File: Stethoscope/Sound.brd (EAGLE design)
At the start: 70 x 70 mm, 24 parts

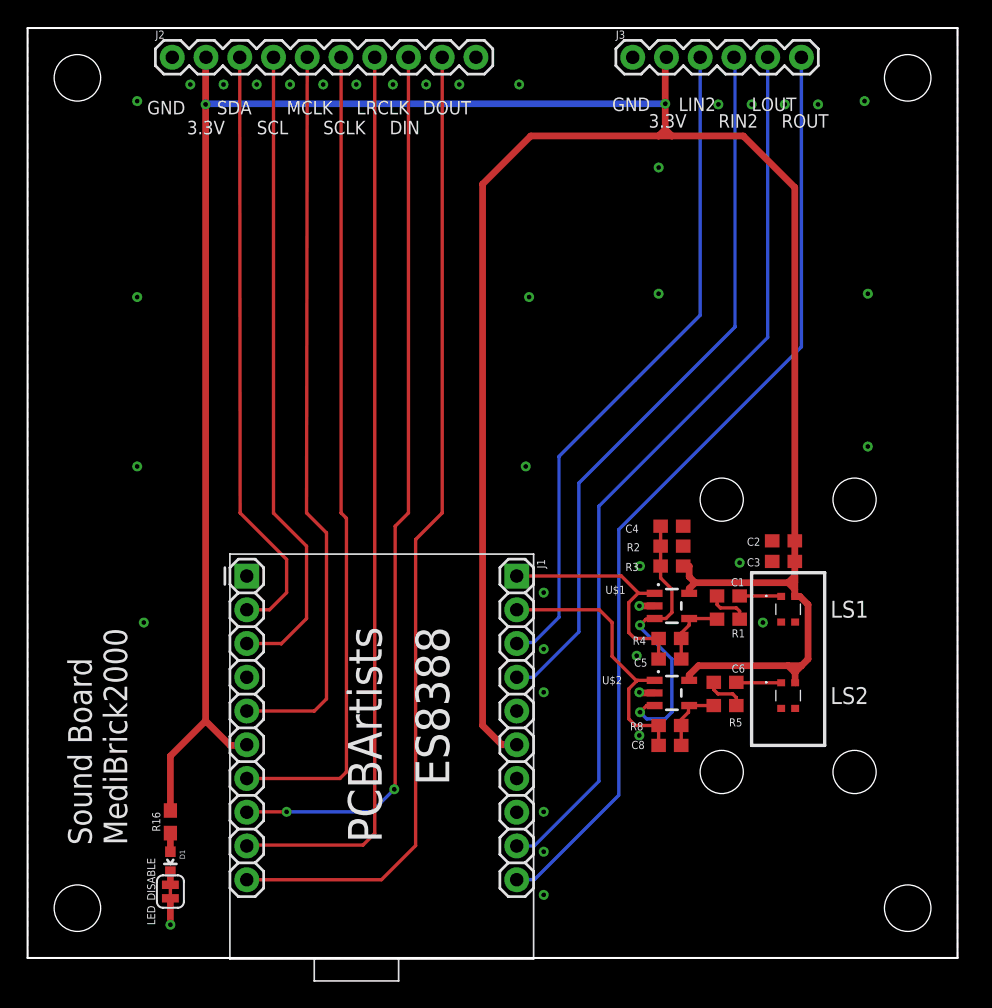
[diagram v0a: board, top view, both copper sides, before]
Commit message: Updated Sound Board
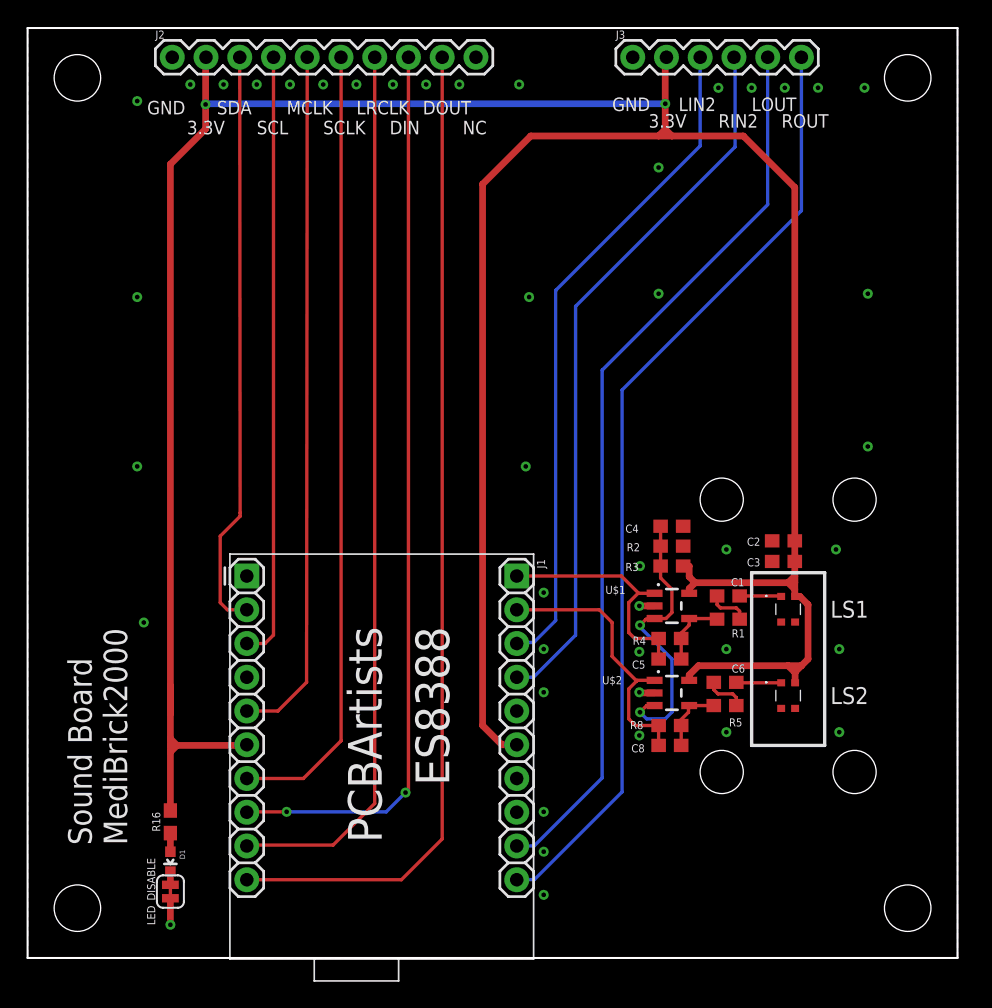
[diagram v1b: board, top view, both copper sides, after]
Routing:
- net 3.3V: track 234.7 -> 240.2 mm
- net N$5: track 55.3 -> 52.4 mm
- net N$4: track 48.6 -> 45.8 mm
- net N$6: track 61.7 -> 59.7 mm
- net N$3: track 45.3 -> 43.9 mm
- net N$9: track 68.3 -> 67.0 mm
- net N$8: track 73.9 -> 74.8 mm
- net N$7: track 67.4 -> 68.1 mm
- net GND: vias 39 -> 43
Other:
- board text added: "NC"

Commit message: Board Updates
All LEDs at same location
Separated analog and digital ground
Updated impedance components
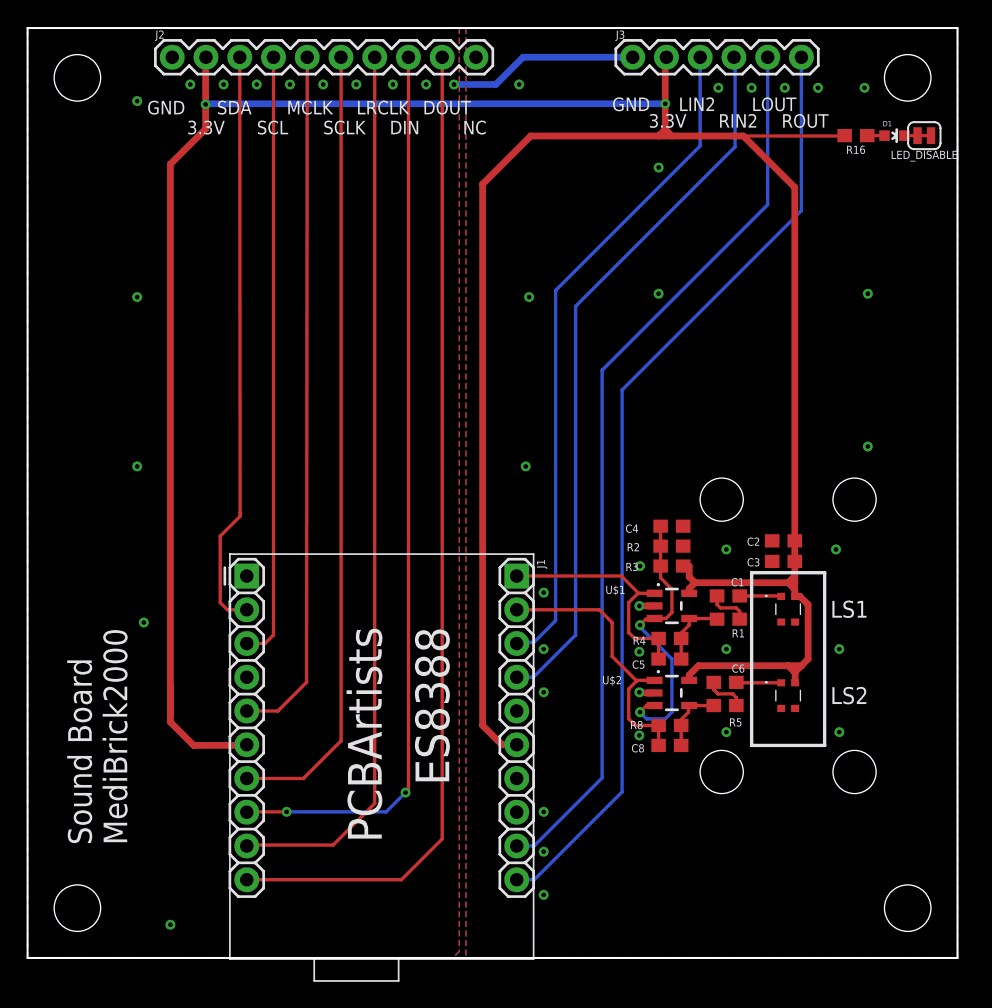
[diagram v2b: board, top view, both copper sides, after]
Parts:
- moved LED_DISABLE 80.4 mm to (67.5, 61.9), turned to 180 degrees
- moved D1 77.2 mm to (65.2, 61.9), turned to 270 degrees
- moved R16 73.0 mm to (62.4, 61.9), turned to 180 degrees
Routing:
- net GND: track 4.31 -> 16.6 mm
- net 3.3V: track 240.2 -> 240.7 mm
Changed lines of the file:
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@@
 <drawing>
 <settings>
-<setting alwaysvectorfont="no"/>
+<setting alwaysvectorfont="yes"/>
 <setting verticaltext="up"/>
 </settings>
@@
 </autorouter>
 <elements>
-<element name="R16" library="SparkFun-Resistors" library_urn="urn:adsk.eagle:library:532" package="0603" package3d_urn="urn:adsk.eagle:package:39650/1" value="1k" x="10.75" y="10.25" smashed="yes" rot="R90">
-<attribute name="NAME" x="9.988" y="10.25" size="0.6096" layer="25" font="vector" ratio="20" rot="R90" align="bottom-center"/>
-<attribute name="PROD_ID" value="RES-07856" x="10.75" y="10.25" size="1.778" layer="27" rot="R90" display="off"/>
-<attribute name="VALUE" x="11.512" y="10.25" size="0.6096" layer="27" font="vector" ratio="20" rot="R90" align="top-center"/>
-</element>
-<element name="D1" library="SparkFun-LED" package="LED-0603" value="RED" x="10.75" y="7.25" smashed="yes" rot="R180">
-<attribute name="NAME" x="11.4485" y="8.139" size="0.4064" layer="25" rot="R270"/>
-<attribute name="PROD_ID" value="DIO-00819" x="13.75" y="0.25" size="1.778" layer="27" rot="R180" display="off"/>
-<attribute name="VALUE" x="9.6705" y="8.266" size="0.4064" layer="27" rot="R270"/>
-</element>
-<element name="LED_DISABLE" library="SparkFun-Jumpers" library_urn="urn:adsk.eagle:library:528" package="SMT-JUMPER_2_NC_TRACE_SILK" package3d_urn="urn:adsk.eagle:package:39281/1" value="JUMPER-SMT_2_NC_TRACE_SILK" x="10.75" y="5" smashed="yes" rot="R90">
-<attribute name="NAME" x="9.607" y="5" size="0.6096" layer="25" font="vector" ratio="20" rot="R90" align="bottom-center"/>
-<attribute name="VALUE" x="11.893" y="5" size="0.6096" layer="27" font="vector" ratio="20" rot="R90" align="top-center" display="off"/>
+<element name="R16" library="SparkFun-Resistors" library_urn="urn:adsk.eagle:library:532" package="0603" package3d_urn="urn:adsk.eagle:package:39650/1" value="1k" x="62.35" y="61.9" smashed="yes" rot="R180">
+<attribute name="NAME" x="62.35" y="61.138" size="0.6096" layer="25" font="vector" ratio="20" rot="R180" align="bottom-center"/>
+<attribute name="PROD_ID" value="RES-07856" x="62.35" y="61.9" size="1.778" layer="27" rot="R180" display="off"/>
+<attribute name="VALUE" x="62.35" y="62.662" size="0.6096" layer="27" font="vector" ratio="20" rot="R180" align="top-center"/>
+</element>
+<element name="D1" library="SparkFun-LED" package="LED-0603" value="RED" x="65.25" y="61.9" smashed="yes" rot="R270">
+<attribute name="NAME" x="64.361" y="62.5985" size="0.4064" layer="25"/>
+<attribute name="PROD_ID" value="DIO-00819" x="72.25" y="64.9" size="1.778" layer="27" rot="R270" display="off"/>
+<attribute name="VALUE" x="64.234" y="60.8205" size="0.4064" layer="27"/>
+</element>
+<element name="LED_DISABLE" library="SparkFun-Jumpers" library_urn="urn:adsk.eagle:library:528" package="SMT-JUMPER_2_NC_TRACE_SILK" package3d_urn="urn:adsk.eagle:package:39281/1" value="JUMPER-SMT_2_NC_TRACE_SILK" x="67.5" y="61.9" smashed="yes" rot="R180">
+<attribute name="NAME" x="67.5" y="60.757" size="0.6096" layer="25" font="vector" ratio="20" rot="R180" align="bottom-center"/>
+<attribute name="VALUE" x="67.5" y="63.043" size="0.6096" layer="27" font="vector" ratio="20" rot="R180" align="top-center" display="off"/>
 </element>
 <element name="FRAME1" library="SparkFun-Aesthetics" library_urn="urn:adsk.eagle:library:507" package="DUMMY" package3d_urn="urn:adsk.eagle:package:37104/1" value="FRAME-LETTERNO_PACKAGE" x="-0.25" y="-5.25" smashed="yes">
@@
 <wire x1="10.75" y1="59.75" x2="13.4" y2="62.4" width="0.508" layer="1"/>
 <wire x1="13.4" y1="62.4" x2="13.4" y2="64.25" width="0.508" layer="1"/>
-<wire x1="10.75" y1="11.1" x2="10.75" y2="15.5" width="0.508" layer="1"/>
-<wire x1="10.75" y1="15.5" x2="10.75" y2="16" width="0.508" layer="1"/>
-<wire x1="10.75" y1="16" x2="10.75" y2="16.5" width="0.508" layer="1"/>
-<wire x1="10.75" y1="16.5" x2="10.75" y2="20.5" width="0.508" layer="1"/>
+<wire x1="10.75" y1="17.75" x2="10.75" y2="20.5" width="0.508" layer="1"/>
 <wire x1="49.8001" y1="27.45" x2="49.8001" y2="27.8001" width="0.508" layer="1"/>
 <wire x1="49.8001" y1="27.8001" x2="50.25" y2="28.25" width="0.508" layer="1"/>
@@
 <wire x1="47.5" y1="61.875" x2="48" y2="62.375" width="0.508" layer="1"/>
 <wire x1="48" y1="62.375" x2="48.5" y2="61.875" width="0.508" layer="1"/>
-<wire x1="16.25" y1="16" x2="11.25" y2="16" width="0.508" layer="1"/>
-<wire x1="10.75" y1="16" x2="11.25" y2="16" width="0.508" layer="1"/>
-<wire x1="11.25" y1="16" x2="10.75" y2="16.5" width="0.508" layer="1"/>
-<wire x1="11.25" y1="16" x2="10.75" y2="15.5" width="0.508" layer="1"/>
+<wire x1="16.5" y1="16.05" x2="16.45" y2="16" width="0.508" layer="1"/>
+<wire x1="16.45" y1="16" x2="12.5" y2="16" width="0.508" layer="1"/>
+<wire x1="12.5" y1="16" x2="10.75" y2="17.75" width="0.508" layer="1"/>
+<wire x1="53.875" y1="61.875" x2="61.475" y2="61.875" width="0.254" layer="1"/>
+<wire x1="61.475" y1="61.875" x2="61.5" y2="61.9" width="0.508" layer="1"/>
 <wire x1="48" y1="64.3" x2="48" y2="62" width="0" layer="19" extent="1-1"/>
 <wire x1="10.75" y1="20.5" x2="10.75" y2="18.391509375" width="0" layer="19" extent="1-1"/>
-<wire x1="16.5" y1="16.05" x2="16.25" y2="16" width="0" layer="19" extent="1-1"/>
 </signal>
 <signal name="GND">
 <via x="8.25" y="64.5" extent="1-16" drill="0.35"/>
 <contactref element="LED_DISABLE" pad="1"/>
-<wire x1="10.75" y1="4.492" x2="10.75" y2="2.5" width="0.508" layer="1"/>
 <via x="10.75" y="2.5" extent="1-16" drill="0.35"/>
-<polygon width="0.508" layer="16" isolate="0.254">
-<vertex x="0" y="70"/>
-<vertex x="0" y="0"/>
+<polygon width="0.1524" layer="16" isolate="0.254">
+<vertex x="33" y="70"/>
+<vertex x="33" y="0"/>
 <vertex x="70" y="0"/>
 <vertex x="70" y="70"/>
 </polygon>
-<polygon width="0.508" layer="1" isolate="0.254">
-<vertex x="0" y="70"/>
-<vertex x="0" y="0"/>
+<polygon width="0.1524" layer="1" isolate="0.254">
+<vertex x="33" y="70"/>
+<vertex x="33" y="0"/>
 <vertex x="70" y="0"/>
 <vertex x="70" y="70"/>
@@
 <via x="27.5" y="65.75" extent="1-16" drill="0.35"/>
 <via x="30" y="65.75" extent="1-16" drill="0.35"/>
-<via x="32.5" y="65.75" extent="1-16" drill="0.35"/>
+<via x="32.1" y="65.75" extent="1-16" drill="0.35"/>
 <contactref element="LS1" pad="3"/>
 <contactref element="LS1" pad="2"/>
@@
 <via x="61.1" y="23.25" extent="1-16" drill="0.35"/>
 <via x="60.85" y="30.75" extent="1-16" drill="0.35"/>
-<wire x1="46.05" y1="20" x2="46.05" y2="16.75" width="0" layer="19" extent="1-1"/>
+<polygon width="0.1524" layer="1" isolate="0.254">
+<vertex x="0" y="70"/>
+<vertex x="32.5" y="70"/>
+<vertex x="32.5" y="0.5"/>
+<vertex x="32" y="0"/>
+<vertex x="0" y="0"/>
+</polygon>
+<polygon width="0.1524" layer="16" isolate="0.254">
+<vertex x="0" y="70"/>
+<vertex x="32.5" y="70"/>
+<vertex x="32.5" y="0.5"/>
+<vertex x="32" y="0"/>
+<vertex x="0" y="0"/>
+</polygon>
+<wire x1="32.1" y1="65.75" x2="35.25" y2="65.75" width="0.508" layer="16"/>
+<wire x1="35.25" y1="65.75" x2="37.3" y2="67.8" width="0.508" layer="16"/>
+<wire x1="37.3" y1="67.8" x2="45.55" y2="67.8" width="0.508" layer="16"/>
 </signal>
 <signal name="N$26">
 <contactref element="R16" pad="1"/>
 <contactref element="D1" pad="A"/>
-<wire x1="10.75" y1="9.4" x2="10.75" y2="8" width="0.508" layer="1"/>
+<wire x1="64.5" y1="61.9" x2="63.2" y2="61.9" width="0.254" layer="1"/>
 </signal>
 <signal name="N$28">
 <contactref element="D1" pad="C"/>
 <contactref element="LED_DISABLE" pad="2"/>
-<wire x1="10.75" y1="5.508" x2="10.75" y2="6.5" width="0.508" layer="1"/>
+<wire x1="66.992" y1="61.9" x2="66" y2="61.9" width="0.254" layer="1"/>
 </signal>
 <signal name="N$3">
